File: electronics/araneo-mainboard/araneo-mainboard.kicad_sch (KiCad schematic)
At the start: 28 parts, among them J1 Conn_01x03_Pin, J10 Conn_01x02_Pin, J11 Conn_01x02_Pin, J2 Conn_01x03_Pin, J3 Conn_01x03_Pin, J4 Conn_01x03_Pin, J5 Conn_01x03_Pin, J6 Conn_01x03_Pin, J7 Conn_01x03_Pin, J8 Conn_01x03_Pin, J9 Conn_01x02_Pin, U1 module_mpu6050, U2 L78M05CDT, U3 BD9C601EFJ

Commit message: electronics: full schematics
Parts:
- added C9: 440uF, symbol Device:C_Polarized
- added F1: Fuse, custom_footprints:3568, symbol Device:Fuse
- added J12: OLED, Connector_PinHeader_2.54mm:PinHeader_1x04_P2.54mm_Vertical, symbol Connector:Conn_01x04_Pin
- added R4, R5, R6: R, Resistor_SMD:R_0603_1608Metric_Pad0.98x0.95mm_HandSolder, symbol Device:R
- added SW1: SW_SPST, Connector_PinHeader_2.54mm:PinHeader_1x02_P2.54mm_Vertical, symbol Switch:SW_SPST
- J10: value Conn_01x02_Pin -> Diode2
- J11: value Conn_01x02_Pin -> Diode3
- J9: value Conn_01x02_Pin -> Diode1
- U1: footprint Usini_Sensors:module_mpu6050 -> usini_sensors:module_mpu6050
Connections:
- net +3V3: now also J12.1 (Pin_1)
- net +5V_LDO: now also A1.39 (VSYS); no longer A1.40 (VBUS)
- net +7.4V: now also F1.1; no longer C3.2, C4.2, U3.2 (VIN), U3.6 (EN)
- net GND: now also C9.2, J12.2 (Pin_2), R4.1, R5.1, R6.1
- net D1: now reaches A1.11 (GPIO8)
- net D1: now also J9.1 (Pin_1)
- net D2: now reaches A1.12 (GPIO9)
- net D2: now also J10.1 (Pin_1)
- net D3: now reaches A1.14 (GPIO10)
- net D3: now also J11.1 (Pin_1)
- net EN: now reaches A1.15 (GPIO11)
- net EN: now also U3.6 (EN)
- net SDA_OLED: now reaches A1.24 (GPIO18)
- net SDA_OLED: now also J12.4 (Pin_4)
- net SCL_OLED: now reaches A1.25 (GPIO19)
- net SCL_OLED: now also J12.3 (Pin_3)
- net at J10.2 (Pin_2): now also R5.2
- net at J11.2 (Pin_2): now also R6.2
- net at J9.2 (Pin_2): now also R4.2
- net SCL renamed SCL_IMU
- net SDA renamed SDA_IMU
- new net: C3.2, C4.2, C9.1, SW1.2 (B), U3.2 (VIN)
- new net: F1.2, SW1.1 (A)
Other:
- note added: "- Obliczyć co trzeba - Dodać footprint dla kondensatora elektrolitycznego - Dobrać: rezystory, włącznik, kondensatory dla LDO"
- note removed: "- Dobrać footprint dla induktora - Obliczyć co trzeba - Włącznik - Dodać rezystory i podłączenia dla diod - Dobrać: rezystory, włącznik, kondensatory dla LDO - OLED"

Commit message: electronics: prepare pcb
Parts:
- added H1, H2, H3, H4: MountingHole_Pad, MountingHole:MountingHole_3.2mm_M3_Pad_Via, symbol Mechanical:MountingHole_Pad
- C3: footprint Capacitor_SMD:C_0603_1608Metric_Pad1.08x0.95mm_HandSolder -> Capacitor_SMD:C_1206_3216Metric_Pad1.33x1.80mm_HandSolder
- C6, C7: footprint Capacitor_SMD:C_0603_1608Metric_Pad1.08x0.95mm_HandSolder -> Capacitor_SMD:C_1210_3225Metric_Pad1.33x2.70mm_HandSolder
- C9: value 440uF -> 470uF; footprint (none) -> Capacitor_THT:CP_Radial_D10.0mm_P5.00mm
- L1: footprint Custom:MPLAL60503R3 -> custom_footprints:INDPM112100X400N
- R4, R5, R6: value R -> 330
- U2: footprint Custom:VREG_L78M05CDT -> custom_footprints:VREG_L78M05CDT
- U3: footprint Custom:SOIC127P600X100-9N -> custom_footprints:SOIC127P600X100-9N
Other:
- note added: "- Obliczyć co trzeba - Dobrać: rezystory, włącznik"
- note removed: "- Obliczyć co trzeba - Dodać footprint dla kondensatora elektrolitycznego - Dobrać: rezystory, włącznik, kondensatory dla LDO"

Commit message: electronics: full PCB
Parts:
- added POWER1: Conn_01x02_Pin, Connector_AMASS:AMASS_XT30U-M_1x02_P5.0mm_Vertical, symbol Connector:Conn_01x02_Pin
- C5: value C -> OPEN
- C8: value C -> 1.5nF
- R1: value R -> 1.2k
- R2: value R -> 7.8k
- R3: value R -> 39k
- SW1: value SW_SPST -> SW
- renumbered U1 to IMU1, J9 to LED1, J10 to LED2, J11 to LED3, J12 to OLED1, J1 to S1, J2 to S2, J3 to S3, J4 to S4, J5 to S5, J6 to S6, J7 to S7, J8 to S8
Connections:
- net +7.4V: now also POWER1.1 (Pin_1)
- net GND: now also C8.2, POWER1.2 (Pin_2); no longer R3.2
- net at U3.5 (COMP): now also R3.1; no longer C8.1
- new net: C8.1, R3.2
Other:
- note removed: "- Obliczyć co trzeba - Dobrać: rezystory, włącznik"
- moved on the sheet: C8, R3

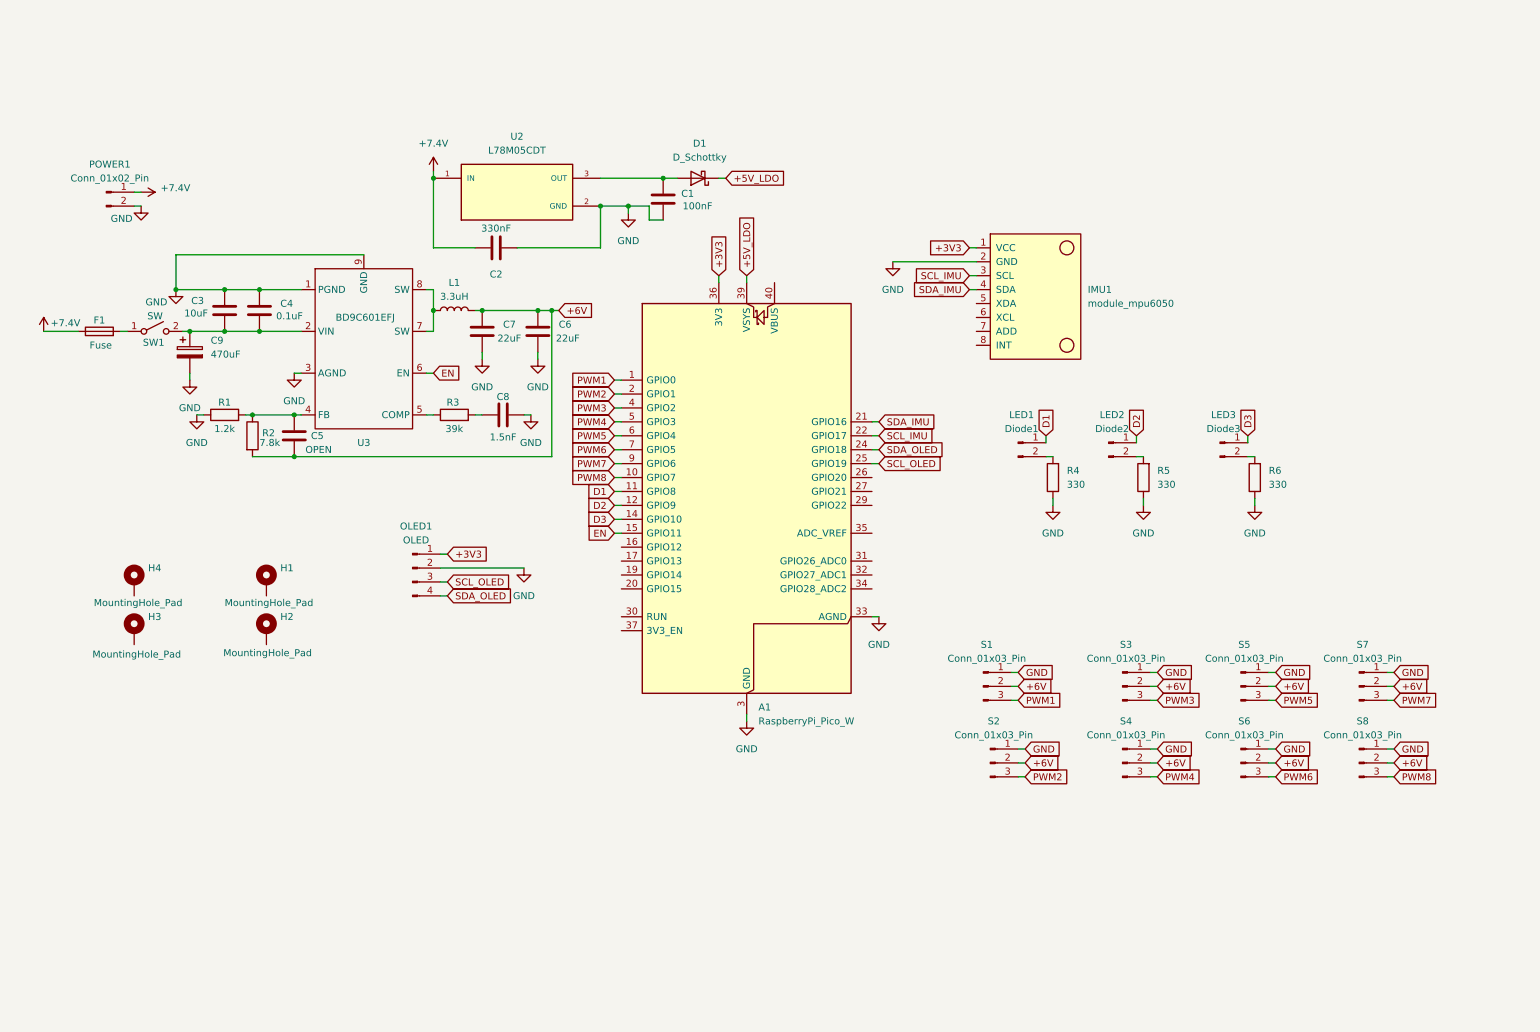
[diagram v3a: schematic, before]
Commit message: electronics: fix schematic and prepare for wiring
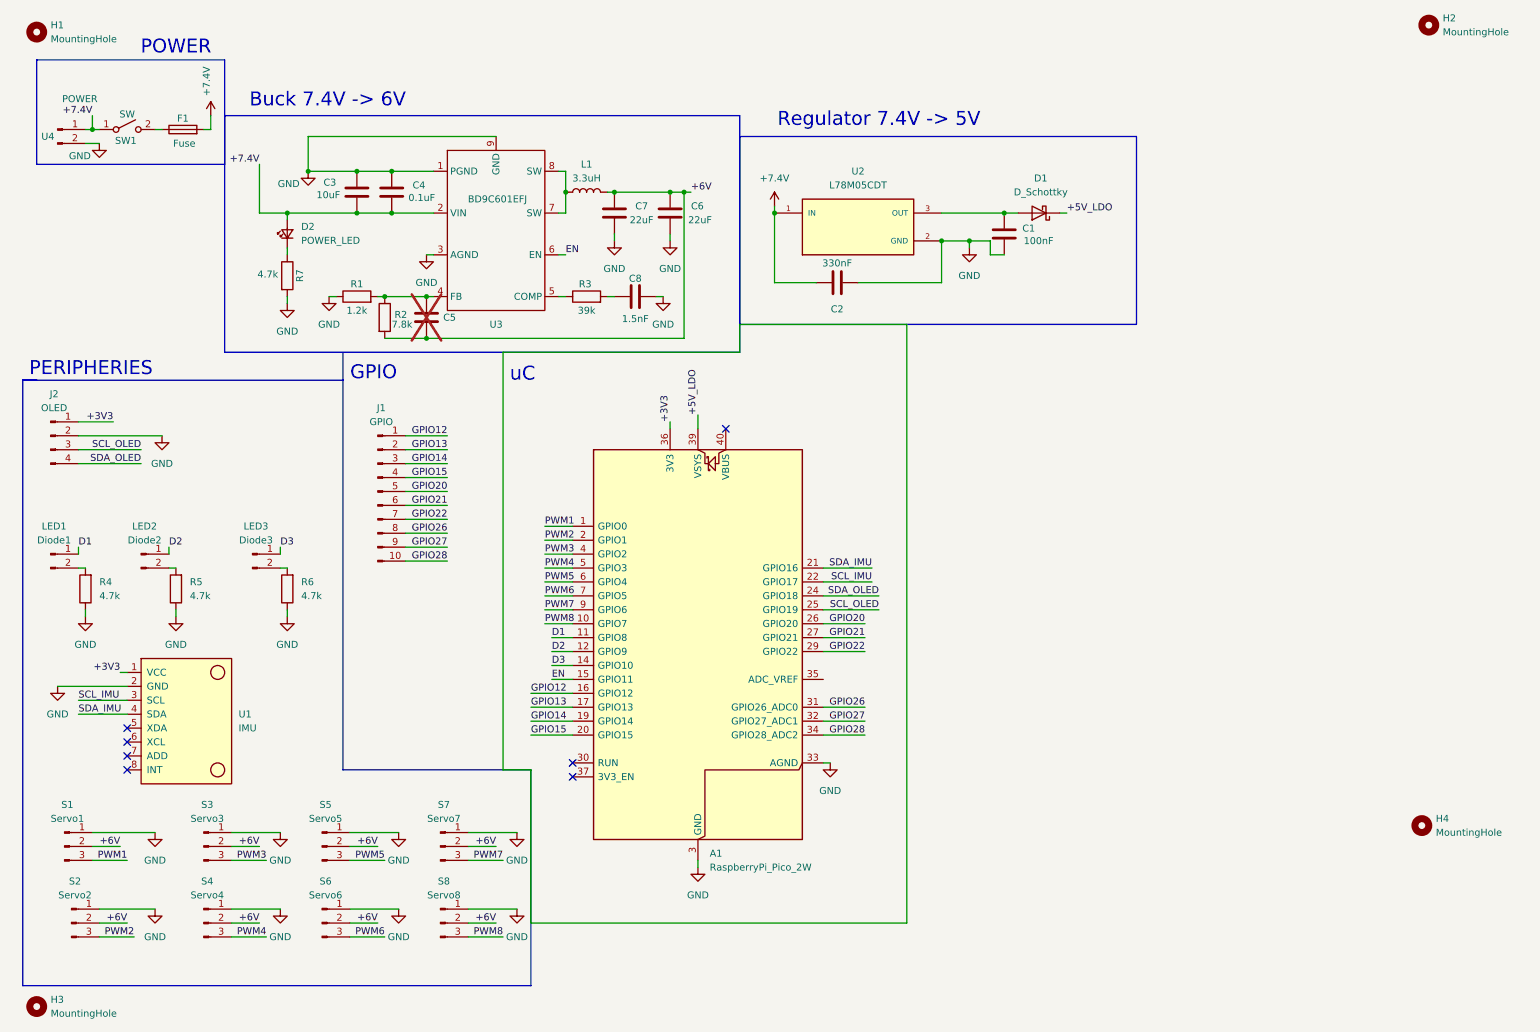
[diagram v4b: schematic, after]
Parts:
- removed C9: 470uF, Capacitor_THT:CP_Radial_D10.0mm_P5.00mm, symbol Device:C_Polarized
- removed H1, H2, H3, H4: MountingHole_Pad, MountingHole:MountingHole_3.2mm_M3_Pad_Via, symbol Mechanical:MountingHole_Pad
- added D2: POWER_LED, PCM_SparkFun-LED:LED_0603_1608Metric, symbol PCM_SparkFun-LED:LED
- added H1, H2, H3, H4: MountingHole, MountingHole:MountingHole_3.2mm_M3, symbol Mechanical:MountingHole
- added J1: GPIO, Connector_PinHeader_2.54mm:PinHeader_1x10_P2.54mm_Vertical, symbol Connector:Conn_01x10_Pin
- added R7: 4.7k, Resistor_SMD:R_0603_1608Metric_Pad0.98x0.95mm_HandSolder, symbol Device:R
- A1: value RaspberryPi_Pico_W -> RaspberryPi_Pico_2W
- C5: now not fitted
- R4, R5, R6: value 330 -> 4.7k
- S1: value Conn_01x03_Pin -> Servo1
- S2: value Conn_01x03_Pin -> Servo2
- S3: value Conn_01x03_Pin -> Servo3
- S4: value Conn_01x03_Pin -> Servo4
- S5: value Conn_01x03_Pin -> Servo5
- S6: value Conn_01x03_Pin -> Servo6
- S7: value Conn_01x03_Pin -> Servo7
- S8: value Conn_01x03_Pin -> Servo8
- U1: renamed from IMU1; value module_mpu6050 -> IMU
- U4: renamed from POWER1; value Conn_01x02_Pin -> POWER
- renumbered OLED1 to J2
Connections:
- net +7.4V: now also C3.2, C4.2, F1.2, SW1.1 (A), U3.2 (VIN), D2.2 (A); no longer F1.1
- net GND: now also R7.2
- net GPIO12: now reaches A1.16 (GPIO12)
- net GPIO12: now also J1.1 (Pin_1)
- net GPIO13: now reaches A1.17 (GPIO13)
- net GPIO13: now also J1.2 (Pin_2)
- net GPIO14: now reaches A1.19 (GPIO14)
- net GPIO14: now also J1.3 (Pin_3)
- net GPIO15: now reaches A1.20 (GPIO15)
- net GPIO15: now also J1.4 (Pin_4)
- net GPIO20: now reaches A1.26 (GPIO20)
- net GPIO20: now also J1.5 (Pin_5)
- net GPIO21: now reaches A1.27 (GPIO21)
- net GPIO21: now also J1.6 (Pin_6)
- net GPIO22: now reaches A1.29 (GPIO22)
- net GPIO22: now also J1.7 (Pin_7)
- net GPIO26: now reaches A1.31 (GPIO26_ADC0)
- net GPIO26: now also J1.8 (Pin_8)
- net GPIO27: now reaches A1.32 (GPIO27_ADC1)
- net GPIO27: now also J1.9 (Pin_9)
- net GPIO28: now reaches A1.34 (GPIO28_ADC2)
- net GPIO28: now also J1.10 (Pin_10)
- new net: D2.1 (K), R7.1
- new net: F1.1, SW1.2 (B)
- no-connect marks 0 -> 7
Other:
- note added: "Buck 7.4V -> 6V"
- note added: "GPIO"
- note added: "PERIPHERIES"
- note added: "POWER"
- note added: "Regulator 7.4V -> 5V"
- note added: "uC"
- moved on the sheet: A1, C1, C2, C3, C4, C6, C7, C8, D1, J2, L1, LED1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

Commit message: electronics: add speaker
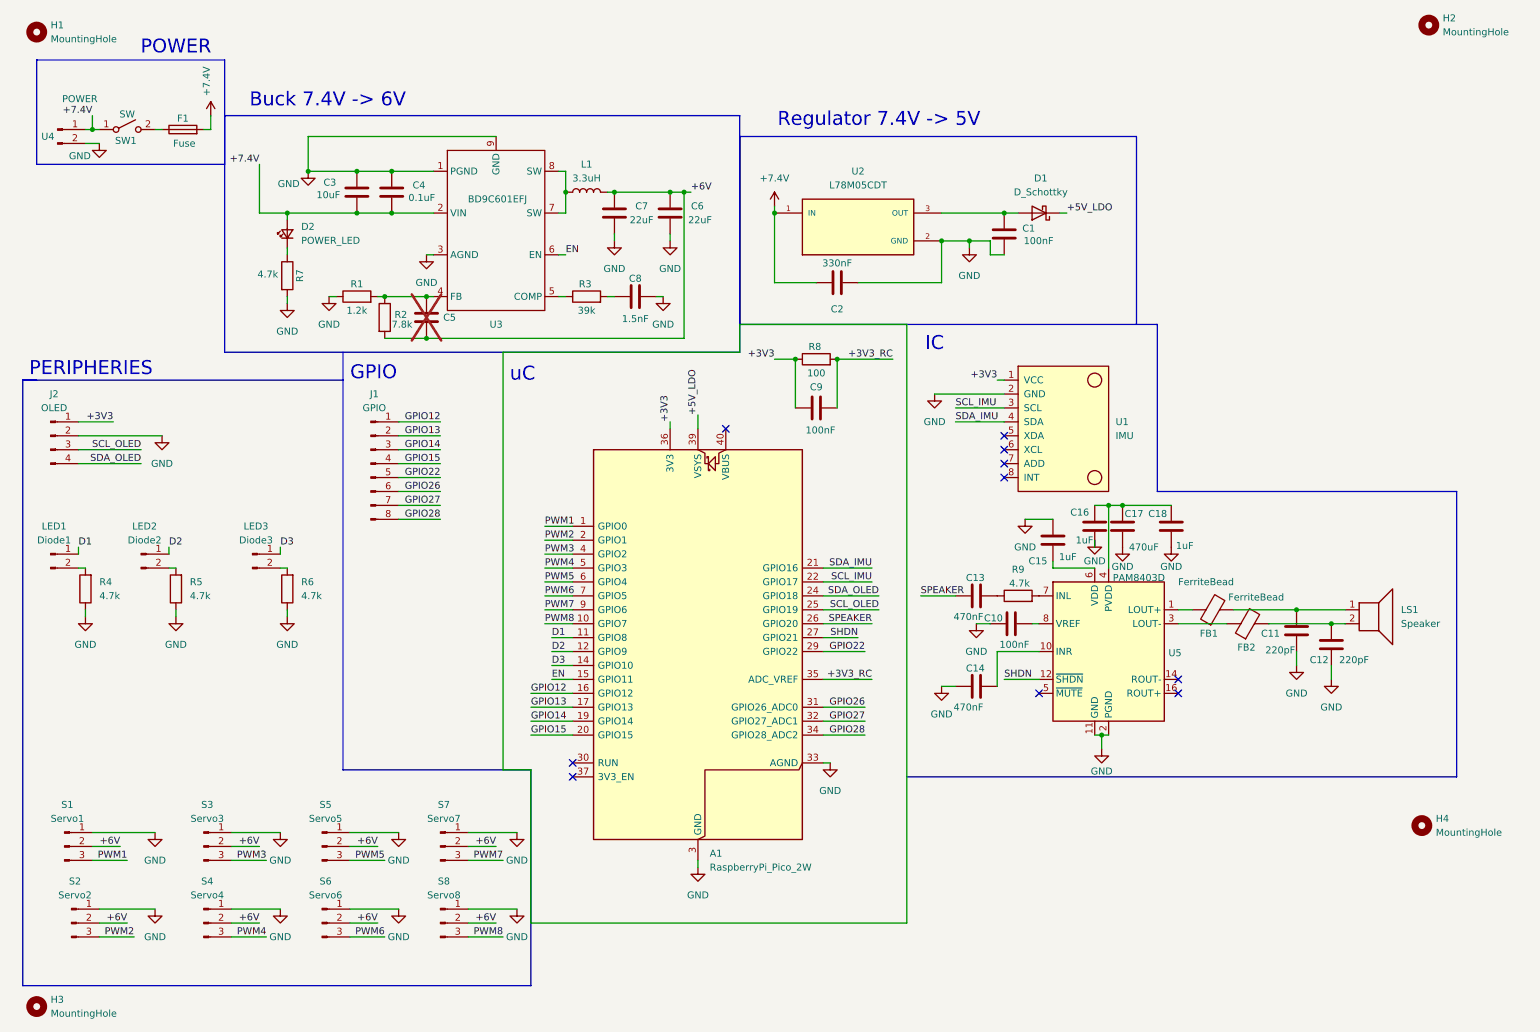
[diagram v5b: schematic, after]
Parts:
- removed J1: GPIO, Connector_PinHeader_2.54mm:PinHeader_1x10_P2.54mm_Vertical, symbol Connector:Conn_01x10_Pin
- added C10, C9: 100nF, Capacitor_SMD:C_0603_1608Metric_Pad1.08x0.95mm_HandSolder, symbol Device:C
- added C11, C12: 220pF, Capacitor_SMD:C_0603_1608Metric_Pad1.08x0.95mm_HandSolder, symbol Device:C
- added C13, C14: 470nF, Capacitor_SMD:C_0603_1608Metric_Pad1.08x0.95mm_HandSolder, symbol Device:C
- added C15, C16, C18: 1uF, symbol Device:C
- added C17: 470uF, symbol Device:C
- added FB1, FB2: FerriteBead, symbol Device:FerriteBead
- added J1: GPIO, Connector_PinHeader_2.54mm:PinHeader_1x08_P2.54mm_Vertical, symbol Connector:Conn_01x08_Pin
- added LS1: Speaker, Connector_Molex:Molex_PicoBlade_53398-0271_1x02-1MP_P1.25mm_Vertical, symbol Device:Speaker
- added R8: 100, Resistor_SMD:R_0603_1608Metric_Pad0.98x0.95mm_HandSolder, symbol Device:R
- added R9: 4.7k, Resistor_SMD:R_0603_1608Metric_Pad0.98x0.95mm_HandSolder, symbol Device:R
- added U5: PAM8403D, Package_SO:SOIC-16_3.9x9.9mm_P1.27mm, symbol Amplifier_Audio:PAM8403D
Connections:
- net +3V3: now also C9.1, R8.1
- net GND: now also C10.1, C11.1, C12.1, C14.1, C15.2, C16.1, C17.1, C18.1, U5.11 (GND), U5.15 (PGND), U5.2 (PGND)
- net GPIO12: now also J1.1 (Pin_1)
- net GPIO13: now also J1.2 (Pin_2)
- net GPIO14: now also J1.3 (Pin_3)
- net GPIO15: now also J1.4 (Pin_4)
- net GPIO22: now also J1.5 (Pin_5)
- net GPIO26: now also J1.6 (Pin_6)
- net GPIO27: now also J1.7 (Pin_7)
- net GPIO28: now also J1.8 (Pin_8)
- net +3V3_RC: now reaches A1.35 (ADC_VREF)
- net +3V3_RC: now also C9.2, R8.2
- net GPIO20 renamed SPEAKER
- net SPEAKER: now also C13.1
- net GPIO21 renamed SHDN
- net SHDN: now also U5.12 (~{SHDN})
- new net: C10.2, U5.8 (VREF)
- new net: FB1.1, U5.1 (LOUT+)
- new net: C11.2, FB1.2, LS1.1
- new net: C16.2, C17.2, C18.2, U5.13 (PVDD), U5.4 (PVDD)
- new net: C14.2, U5.10 (INR)
- new net: FB2.1, U5.3 (LOUT-)
- new net: C15.1, U5.6 (VDD)
- new net: R9.2, U5.7 (INL)
- new net: C13.2, R9.1
- new net: C12.2, FB2.2, LS1.2
- no-connect marks 7 -> 10
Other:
- note added: "IC"
- moved on the sheet: U1
